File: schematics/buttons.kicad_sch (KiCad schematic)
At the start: 25 parts, among them SW2 SW_SPST, SW3 SW_SPST, SW4 SW_SPST, SW5 SW_SPST, SW6 SW_SPST, SW7 SW_SPST, SW8 SW_SPST, SW9 SW_SPST, U2 ADS1115IDGS

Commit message: Update README
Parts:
- added U5: PCF8574T, Package_SO:SOIC-16W_7.5x10.3mm_P1.27mm, symbol Interface_Expansion:PCF8574T
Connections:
- net +3.3V: now also U2.8 (VDD), U5.16 (VDD)
- net GND: now also U2.3 (GND), U5.8 (GND)
- net at SW5.1 (A): now also U5.7 (P3)
- net SCL: now reaches U2.10 (SCL)
- net SCL: now also U5.14 (SCL)
- net SDA: now reaches U2.9 (SDA)
- net SDA: now also U5.15 (SDA)
- net at SW9.1 (A): now also U5.12 (P7)
- net at SW3.1 (A): now also U5.4 (P0)
- net at SW4.1 (A): now also U5.6 (P2)
- net at SW6.1 (A): now also U5.9 (P4)
- net at SW2.1 (A): now also U5.5 (P1)
- net at SW7.1 (A): now also U5.10 (P5)
- net at SW8.1 (A): now also U5.11 (P6)
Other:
- moved on the sheet: D1, D2, D3, D6, FAD1, FAD2, FAD3, FAD4, R10, R11, R12, R13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

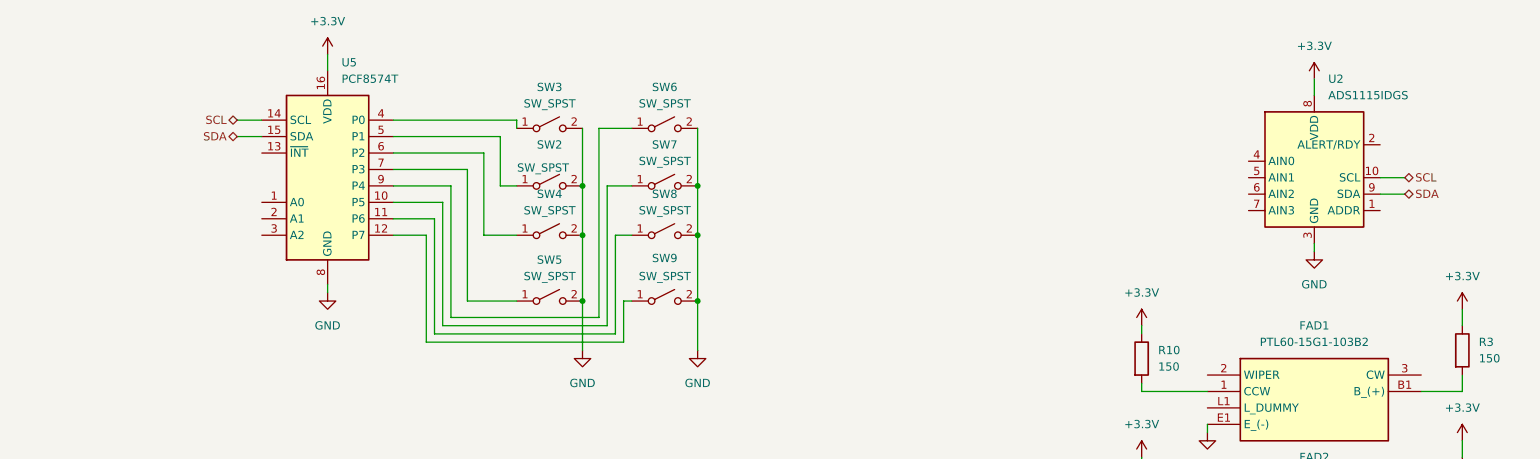
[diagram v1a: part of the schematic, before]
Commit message: Wire buttons
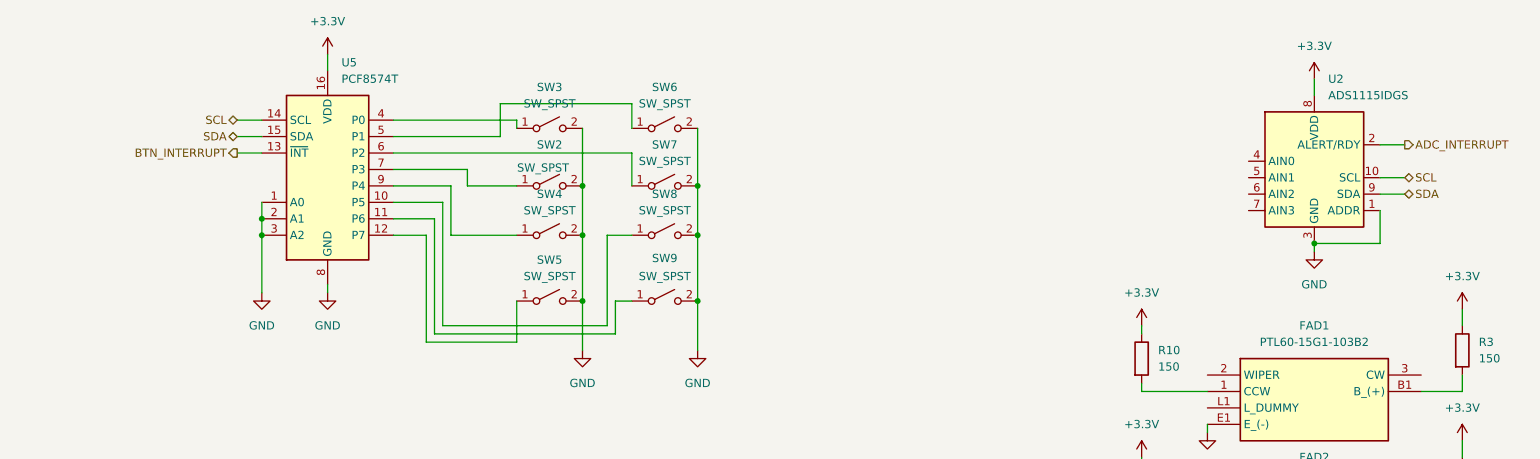
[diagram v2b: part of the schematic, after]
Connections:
- net GND: now also U2.1 (ADDR), U5.1 (A0), U5.2 (A1), U5.3 (A2)
- net at SW5.1 (A): now also U5.12 (P7); no longer U5.7 (P3)
- net ADC_INTERRUPT: now reaches U2.2 (ALERT/RDY)
- net at SW9.1 (A): now also U5.11 (P6); no longer U5.12 (P7)
- net at SW4.1 (A): now also U5.9 (P4); no longer U5.6 (P2)
- net at SW6.1 (A): now also U5.5 (P1); no longer U5.9 (P4)
- net at SW2.1 (A): now also U5.7 (P3); no longer U5.5 (P1)
- net at SW7.1 (A): now also U5.6 (P2); no longer U5.10 (P5)
- net at SW8.1 (A): now also U5.10 (P5); no longer U5.11 (P6)
- net BTN_INTERRUPT: now reaches U5.13 (~{INT})
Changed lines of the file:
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@@
 	)
 	(junction
+		(at 64.77 55.88)
+		(diameter 0)
+		(color 0 0 0 0)
+	)
+	(junction
 		(at 40.64 113.03)
 		(diameter 0)
@@
 	)
 	(junction
+		(at 227.33 57.15)
+		(diameter 0)
+		(color 0 0 0 0)
+	)
+	(junction
 		(at 132.08 66.04)
 		(diameter 0)
@@
 	)
 	(junction
+		(at 64.77 53.34)
+		(diameter 0)
+		(color 0 0 0 0)
+	)
+	(junction
 		(at 132.08 55.88)
 		(diameter 0)
@@
 	(wire
 		(pts
-			(xy 93.98 68.58) (xy 116.84 68.58)
+			(xy 64.77 50.8) (xy 64.77 53.34)
+		)
+		(stroke
+			(width 0)
+			(type default)
+		)
+	)
+	(wire
+		(pts
+			(xy 96.52 48.26) (xy 96.52 45.72)
+		)
+		(stroke
+			(width 0)
+			(type default)
+		)
+	)
+	(wire
+		(pts
+			(xy 101.6 40.64) (xy 101.6 35.56)
 		)
 		(stroke
@@
 	(wire
 		(pts
+			(xy 104.14 66.04) (xy 104.14 72.39)
+		)
+		(stroke
+			(width 0)
+			(type default)
+		)
+	)
+	(wire
+		(pts
 			(xy 210.82 105.41) (xy 209.55 105.41)
 		)
@@
 	(wire
 		(pts
-			(xy 40.64 113.03) (xy 55.88 113.03)
+			(xy 118.11 69.85) (xy 118.11 55.88)
 		)
 		(stroke
@@
 	(wire
 		(pts
-			(xy 92.71 69.85) (xy 92.71 50.8)
+			(xy 40.64 113.03) (xy 55.88 113.03)
 		)
 		(stroke
@@
 	(wire
 		(pts
-			(xy 116.84 68.58) (xy 116.84 39.37)
+			(xy 92.71 69.85) (xy 92.71 50.8)
 		)
 		(stroke
@@
 	(wire
 		(pts
+			(xy 121.92 35.56) (xy 121.92 39.37)
+		)
+		(stroke
+			(width 0)
+			(type default)
+		)
+	)
+	(wire
+		(pts
 			(xy 237.49 49.53) (xy 241.3 49.53)
 		)
@@
 	(wire
 		(pts
+			(xy 60.96 43.18) (xy 64.77 43.18)
+		)
+		(stroke
+			(width 0)
+			(type default)
+		)
+	)
+	(wire
+		(pts
 			(xy 132.08 39.37) (xy 132.08 48.26)
 		)
@@
 	(wire
 		(pts
-			(xy 85.09 45.72) (xy 96.52 45.72)
+			(xy 237.49 57.15) (xy 227.33 57.15)
 		)
 		(stroke
@@
 	(wire
 		(pts
-			(xy 200.66 142.24) (xy 210.82 142.24)
+			(xy 85.09 45.72) (xy 96.52 45.72)
 		)
 		(stroke
@@
 	(wire
 		(pts
-			(xy 55.88 113.03) (xy 55.88 130.81)
+			(xy 200.66 142.24) (xy 210.82 142.24)
 		)
 		(stroke
@@
 	(wire
 		(pts
-			(xy 243.84 120.65) (xy 250.19 120.65)
+			(xy 55.88 113.03) (xy 55.88 130.81)
 		)
 		(stroke
@@
 	(wire
 		(pts
-			(xy 121.92 48.26) (xy 118.11 48.26)
+			(xy 243.84 120.65) (xy 250.19 120.65)
 		)
 		(stroke
@@
 	(wire
 		(pts
-			(xy 118.11 48.26) (xy 118.11 69.85)
+			(xy 29.21 120.65) (xy 33.02 120.65)
 		)
 		(stroke
@@
 	(wire
 		(pts
-			(xy 29.21 120.65) (xy 33.02 120.65)
+			(xy 96.52 48.26) (xy 104.14 48.26)
 		)
 		(stroke
@@
 	(wire
 		(pts
-			(xy 210.82 125.73) (xy 209.55 125.73)
+			(xy 93.98 55.88) (xy 104.14 55.88)
 		)
 		(stroke
@@
 	(wire
 		(pts
-			(xy 85.09 48.26) (xy 93.98 48.26)
+			(xy 210.82 125.73) (xy 209.55 125.73)
 		)
 		(stroke
@@
 	(wire
 		(pts
-			(xy 120.65 72.39) (xy 90.17 72.39)
+			(xy 85.09 48.26) (xy 93.98 48.26)
 		)
 		(stroke
@@
 	(wire
 		(pts
-			(xy 74.93 63.5) (xy 74.93 64.77)
+			(xy 119.38 66.04) (xy 121.92 66.04)
 		)
 		(stroke
@@
 	(wire
 		(pts
-			(xy 119.38 55.88) (xy 121.92 55.88)
+			(xy 74.93 63.5) (xy 74.93 64.77)
 		)
 		(stroke
@@
 	(wire
 		(pts
-			(xy 78.74 161.29) (xy 78.74 177.8)
+			(xy 64.77 55.88) (xy 64.77 64.77)
 		)
 		(stroke
@@
 	(wire
 		(pts
-			(xy 91.44 71.12) (xy 119.38 71.12)
+			(xy 78.74 161.29) (xy 78.74 177.8)
 		)
 		(stroke
@@
 	(wire
 		(pts
-			(xy 227.33 31.75) (xy 227.33 34.29)
+			(xy 91.44 71.12) (xy 119.38 71.12)
 		)
 		(stroke
@@
 	(wire
 		(pts
-			(xy 78.74 177.8) (xy 82.55 177.8)
+			(xy 227.33 31.75) (xy 227.33 34.29)
 		)
 		(stroke
@@
 	(wire
 		(pts
-			(xy 200.66 110.49) (xy 200.66 111.76)
+			(xy 78.74 177.8) (xy 82.55 177.8)
 		)
 		(stroke
@@
 	(wire
 		(pts
-			(xy 119.38 71.12) (xy 119.38 55.88)
+			(xy 200.66 110.49) (xy 200.66 111.76)
 		)
 		(stroke
@@
 	(wire
 		(pts
-			(xy 99.06 55.88) (xy 104.14 55.88)
-		)
-		(stroke
-			(width 0)
-			(type default)
-		)
-	)
-	(wire
-		(pts
-			(xy 120.65 66.04) (xy 120.65 72.39)
+			(xy 237.49 41.91) (xy 241.3 41.91)
 		)
 		(stroke
@@
 	(wire
 		(pts
-			(xy 101.6 48.26) (xy 104.14 48.26)
+			(xy 71.12 153.67) (xy 90.17 153.67)
 		)
 		(stroke
@@
 	(wire
 		(pts
-			(xy 71.12 153.67) (xy 90.17 153.67)
+			(xy 60.96 38.1) (xy 64.77 38.1)
 		)
 		(stroke
@@
 	(wire
 		(pts
-			(xy 101.6 40.64) (xy 101.6 48.26)
+			(xy 85.09 55.88) (xy 90.17 55.88)
 		)
 		(stroke
@@
 	(wire
 		(pts
-			(xy 60.96 38.1) (xy 64.77 38.1)
+			(xy 121.92 48.26) (xy 121.92 43.18)
 		)
 		(stroke
@@
 	(wire
 		(pts
-			(xy 96.52 45.72) (xy 96.52 66.04)
+			(xy 237.49 52.07) (xy 237.49 57.15)
 		)
 		(stroke
@@
 	(wire
 		(pts
-			(xy 85.09 55.88) (xy 90.17 55.88)
+			(xy 250.19 67.31) (xy 250.19 69.85)
 		)
 		(stroke
@@
 	(wire
 		(pts
-			(xy 116.84 39.37) (xy 121.92 39.37)
+			(xy 114.3 48.26) (xy 114.3 55.88)
 		)
 		(stroke
@@
 	(wire
 		(pts
-			(xy 250.19 67.31) (xy 250.19 69.85)
+			(xy 119.38 71.12) (xy 119.38 66.04)
 		)
 		(stroke
@@
 	(wire
 		(pts
-			(xy 114.3 48.26) (xy 114.3 55.88)
+			(xy 71.12 168.91) (xy 71.12 172.72)
 		)
 		(stroke
@@
 	(wire
 		(pts
-			(xy 71.12 168.91) (xy 71.12 172.72)
+			(xy 104.14 72.39) (xy 90.17 72.39)
 		)
 		(stroke
@@
 	(wire
 		(pts
-			(xy 96.52 66.04) (xy 104.14 66.04)
+			(xy 118.11 55.88) (xy 121.92 55.88)
 		)
 		(stroke
@@
 	(wire
 		(pts
-			(xy 121.92 66.04) (xy 120.65 66.04)
+			(xy 104.14 38.1) (xy 104.14 39.37)
 		)
 		(stroke
@@
 	(wire
 		(pts
-			(xy 99.06 43.18) (xy 99.06 55.88)
+			(xy 101.6 35.56) (xy 121.92 35.56)
 		)
 		(stroke
@@
 	(wire
 		(pts
-			(xy 104.14 38.1) (xy 104.14 39.37)
+			(xy 250.19 80.01) (xy 250.19 77.47)
 		)
 		(stroke
@@
 	(wire
 		(pts
-			(xy 250.19 80.01) (xy 250.19 77.47)
+			(xy 64.77 53.34) (xy 64.77 55.88)
 		)
 		(stroke
@@
 	(wire
 		(pts
-			(xy 85.09 43.18) (xy 99.06 43.18)
+			(xy 85.09 43.18) (xy 121.92 43.18)
 		)
 		(stroke
@@
 	(wire
 		(pts
-			(xy 93.98 48.26) (xy 93.98 68.58)
+			(xy 93.98 48.26) (xy 93.98 55.88)
 		)
 		(stroke
@@
 		)
 	)
+	(hierarchical_label "ADC_INTERRUPT"
+		(shape output)
+		(at 241.3 41.91 0)
+		(effects
+			(font
+				(size 1.27 1.27)
+			)
+			(justify left)
+		)
+	)
 	(hierarchical_label "SCL"
 		(shape bidirectional)
@@
 		)
 	)
+	(hierarchical_label "BTN_INTERRUPT"
+		(shape output)
+		(at 60.96 43.18 180)
+		(effects
+			(font
+				(size 1.27 1.27)
+			)
+			(justify right)
+		)
+	)
 	(symbol
 		(lib_id "Device:R")
@@
 					(unit 1)
 				)
+			)
+		)
+	)
+	(symbol
+		(lib_id "power:GND")
+		(at 64.77 64.77 0)
+		(unit 1)
+		(exclude_from_sim no)
+		(in_bom yes)
+		(on_board yes)
+		(dnp no)
+		(fields_autoplaced yes)
+		(property "Reference" "#PWR040"
+			(at 64.77 71.12 0)
+			(effects
+				(font
+					(size 1.27 1.27)
+				)
+				(hide yes)
+			)
+		)
+		(property "Value" "GND"
+			(at 64.77 69.85 0)
+			(effects
+				(font
+					(size 1.27 1.27)
+				)
+			)
+		)
+		(property "Footprint" ""
+			(at 64.77 64.77 0)
+			(effects
+				(font
+					(size 1.27 1.27)
+				)
+				(hide yes)
+			)
+		)
+		(property "Datasheet" ""
+			(at 64.77 64.77 0)
+			(effects
+				(font
+					(size 1.27 1.27)
+				)
+				(hide yes)
+			)
+		)
+		(property "Description" "Power symbol creates a global label with name \"GND\" , ground"
+			(at 64.77 64.77 0)
+			(effects
+				(font
+					(size 1.27 1.27)
+				)
+				(hide yes)
+			)
+		)
+		(pin "1"
+		)
+		(instances
+			(project "miixer"
+				(path "/f2af4cd4-99cf-4d01-92f6-6413371e0fe3/5611f13c-04e1-436b-9132-43ac5c8df051"
+					(reference "#PWR040")
+					(unit 1)
+				)

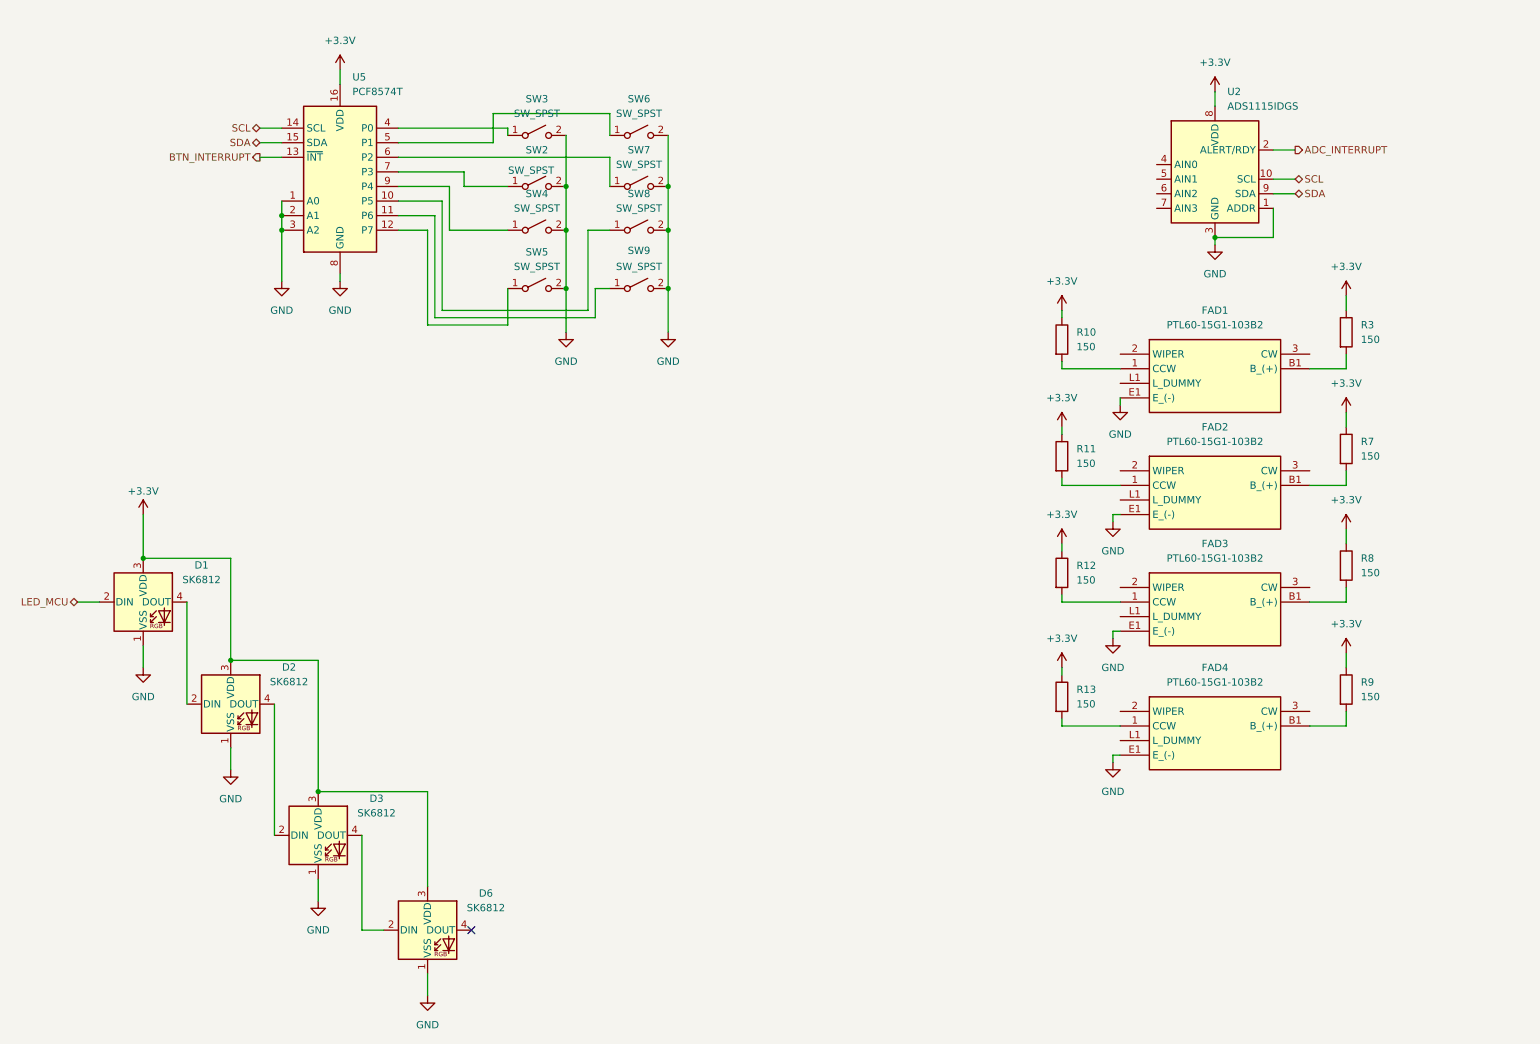
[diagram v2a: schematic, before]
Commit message: Add LED driver ic TLC59208F
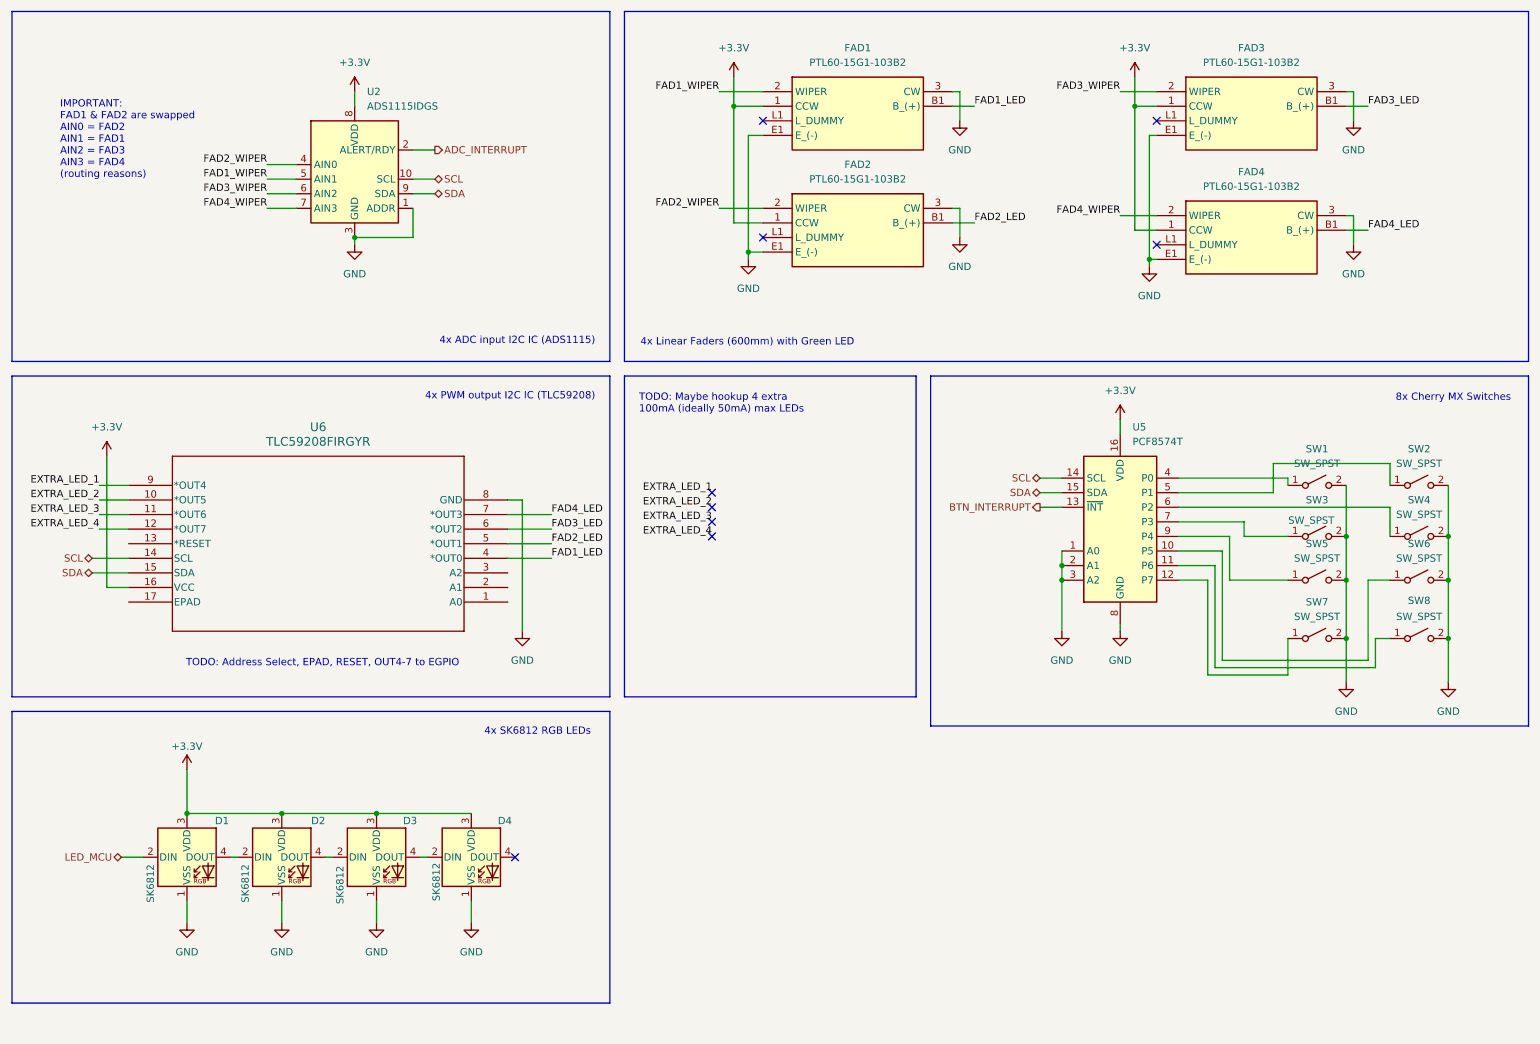
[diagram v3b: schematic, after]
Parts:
- removed R10, R11, R12, R13, R3, R7, R8, R9: 150, symbol Device:R
- added U6: TLC59208FIRGYR, RGY16_2P55X2P05, symbol 2025-07-19_04-59-13:TLC59208FIRGYR
- renumbered D6 to D4, SW3 to SW1, SW6 to SW2, SW2 to SW3, SW7 to SW4, SW4 to SW5, SW8 to SW6, SW5 to SW7, SW9 to SW8
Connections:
- net +3.3V: now also FAD1.1 (CCW), FAD2.1 (CCW), FAD3.1 (CCW), FAD4.1 (CCW), U6.16 (VCC)
- net GND: now also FAD1.3 (CW), FAD2.3 (CW), FAD3.3 (CW), FAD4.3 (CW), U6.8 (GND)
- net SCL: now also U6.14 (SCL)
- net SDA: now also U6.15 (SDA)
- net FAD2_WIPER: now reaches FAD2.2 (WIPER)
- net FAD2_WIPER: now also U2.4 (AIN0)
- net FAD2_LED: now reaches FAD2.B1 (B_(+))
- net FAD2_LED: now also U6.5 (*OUT1)
- net FAD1_WIPER: now reaches U2.5 (AIN1)
- net FAD1_WIPER: now also FAD1.2 (WIPER)
- net FAD3_WIPER: now reaches U2.6 (AIN2)
- net FAD3_WIPER: now also FAD3.2 (WIPER)
- net FAD4_WIPER: now reaches U2.7 (AIN3)
- net FAD4_WIPER: now also FAD4.2 (WIPER)
- net FAD4_LED: now reaches FAD4.B1 (B_(+))
- net FAD4_LED: now also U6.7 (*OUT3)
- net FAD3_LED: now reaches FAD3.B1 (B_(+))
- net FAD3_LED: now also U6.6 (*OUT2)
- net FAD1_LED: now reaches FAD1.B1 (B_(+))
- net FAD1_LED: now also U6.4 (*OUT0)
- new net EXTRA_LED_1: U6.9 (*OUT4)
- new net EXTRA_LED_2: U6.10 (*OUT5)
- new net EXTRA_LED_3: U6.11 (*OUT6)
- new net EXTRA_LED_4: U6.12 (*OUT7)
- no-connect marks 1 -> 9
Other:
- note added: "4x ADC input I2C IC (ADS1115)"
- note added: "4x Linear Faders (600mm) with Green LED"
- note added: "4x PWM output I2C IC (TLC59208)"
- note added: "4x SK6812 RGB LEDs"
- note added: "8x Cherry MX Switches"
- note added: "IMPORTANT: FAD1 & FAD2 are swapped AIN0 = FAD2 AIN1 = FAD1 AIN2 = FAD3 AIN3 = FAD4 (routing reasons)"
- note added: "TODO: Address Select, EPAD, RESET, OUT4-7 to EGPIO"
- note added: "TODO: Maybe hookup 4 extra 100mA (ideally 50mA) max LEDs"
- moved on the sheet: D1, D2, D3, D4, FAD1, FAD2, FAD3, FAD4, SW1, SW2, SW3, SW4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
